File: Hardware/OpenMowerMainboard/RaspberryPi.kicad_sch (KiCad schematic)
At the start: 10 parts, among them J21 Raspberry_Pi_2_3, J22 Conn_02x04_Odd_Even, M1 Fan, Q3 BSS138, U3 SIP32509DT

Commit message: BoM data added to kicad - results exported to .xlsx file
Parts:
- D1: LCSC (none) -> C541613; Part Number (none) -> AS160-M; Stock_PN (none) -> D-AS160-M
- J21: Digikey (none) -> S5729-ND; Part Number (none) -> NPPC202KFMS-RC; Stock_PN (none) -> J-SMD-2x20-.1F
- J22: LCSC (none) -> C2894965; Part Number (none) -> PZ254-2-04-Z-8.5; Stock_PN (none) -> J-TH-2x4-.1
- M1: LCSC (none) -> C2935908; Part Number (none) -> DZ254R-11-02-63; Stock_PN (none) -> J-TH-1x2-.1
- Q3: LCSC (none) -> C360338; Part Number (none) -> AP2300; Stock_PN (none) -> Q-AP2300
- R1, R2, R4: Digikey (none) -> 738-RMCF0805FG10K0CT-ND; Part Number (none) -> RMCF0805FG10K0; Stock_PN (none) -> R-805-10K-.125W-1%
- R5: Digikey (none) -> 311-150CRCT-ND; Part Number (none) -> RC0805FR-07150RL; Stock_PN (none) -> R-805-150-.125W-1%
- U3: Digikey (none) -> SIP32509DT-T1-GE3CT-ND; Part Number (none) -> SIP32509DT-T1-GE3; Stock_PN (none) -> U-SIP32509
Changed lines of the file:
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@@
+      (effects (font (size 1.27 1.27)) hide)
+    )
+    (property "LCSC" "C2935908" (id 4) (at 116.84 36.83 0)
+      (effects (font (size 1.27 1.27)) hide)
+    )
+    (property "Part Number" "DZ254R-11-02-63" (id 5) (at 116.84 36.83 0)
+      (effects (font (size 1.27 1.27)) hide)
+    )
+    (property "Stock_PN" "J-TH-1x2-.1" (id 6) (at 116.84 36.83 0)
       (effects (font (size 1.27 1.27)) hide)
     )
@@
     )
     (property "Datasheet" "~" (id 3) (at 107.95 35.56 0)
+      (effects (font (size 1.27 1.27)) hide)
+    )
+    (property "LCSC" "C541613" (id 4) (at 107.95 35.56 0)
+      (effects (font (size 1.27 1.27)) hide)
+    )
+    (property "Part Number" "AS160-M" (id 5) (at 107.95 35.56 0)
+      (effects (font (size 1.27 1.27)) hide)
+    )
+    (property "Stock_PN" "D-AS160-M" (id 6) (at 107.95 35.56 0)
       (effects (font (size 1.27 1.27)) hide)
     )
@@
     )
     (property "Datasheet" "~" (id 3) (at 184.15 152.4 0)
+      (effects (font (size 1.27 1.27)) hide)
+    )
+    (property "Digikey" "738-RMCF0805FG10K0CT-ND" (id 4) (at 184.15 152.4 0)
+      (effects (font (size 1.27 1.27)) hide)
+    )
+    (property "Part Number" "RMCF0805FG10K0" (id 5) (at 184.15 152.4 0)
+      (effects (font (size 1.27 1.27)) hide)
+    )
+    (property "Stock_PN" "R-805-10K-.125W-1%" (id 6) (at 184.15 152.4 0)
       (effects (font (size 1.27 1.27)) hide)
     )
@@
     )
     (property "Datasheet" "~" (id 3) (at 57.785 144.145 0)
+      (effects (font (size 1.27 1.27)) hide)
+    )
+    (property "LCSC" "C2894965" (id 4) (at 57.785 144.145 0)
+      (effects (font (size 1.27 1.27)) hide)
+    )
+    (property "Part Number" "	PZ254-2-04-Z-8.5" (id 5) (at 57.785 144.145 0)
+      (effects (font (size 1.27 1.27)) hide)
+    )
+    (property "Stock_PN" "J-TH-2x4-.1" (id 6) (at 57.785 144.145 0)
       (effects (font (size 1.27 1.27)) hide)
     )
@@
       (effects (font (size 1.27 1.27)) hide)
     )
+    (property "Digikey" "SIP32509DT-T1-GE3CT-ND" (id 4) (at 166.37 17.78 0)
+      (effects (font (size 1.27 1.27)) hide)
+    )
+    (property "Part Number" "SIP32509DT-T1-GE3" (id 5) (at 166.37 17.78 0)
+      (effects (font (size 1.27 1.27)) hide)
+    )
+    (property "Stock_PN" "U-SIP32509" (id 6) (at 166.37 17.78 0)
+      (effects (font (size 1.27 1.27)) hide)
+    )
     (pin "1")
     (pin "2")
@@
       (effects (font (size 1.27 1.27)) hide)
     )
+    (property "Stock_PN" "R-805-150-.125W-1%" (id 4) (at 101.6 49.53 0)
+      (effects (font (size 1.27 1.27)) hide)
+    )
+    (property "Digikey" "311-150CRCT-ND" (id 5) (at 101.6 49.53 0)
+      (effects (font (size 1.27 1.27)) hide)
+    )
+    (property "Part Number" "RC0805FR-07150RL" (id 6) (at 101.6 49.53 0)
+      (effects (font (size 1.27 1.27)) hide)
+    )
     (pin "1")
     (pin "2")
@@
       (effects (font (size 1.27 1.27)) (justify left) hide)
     )
+    (property "LCSC" "C360338" (id 4) (at 114.3 49.53 0)
+      (effects (font (size 1.27 1.27)) hide)
+    )
+    (property "Part Number" "AP2300" (id 5) (at 114.3 49.53 0)
+      (effects (font (size 1.27 1.27)) hide)
+    )
+    (property "Stock_PN" "Q-AP2300" (id 6) (at 114.3 49.53 0)
+      (effects (font (size 1.27 1.27)) hide)
+    )
     (pin "1")
     (pin "2")
@@
       (effects (font (size 1.27 1.27)) hide)
     )
+    (property "Digikey" "738-RMCF0805FG10K0CT-ND" (id 4) (at 93.98 57.15 0)
+      (effects (font (size 1.27 1.27)) hide)
+    )
+    (property "Part Number" "RMCF0805FG10K0" (id 5) (at 93.98 57.15 0)
+      (effects (font (size 1.27 1.27)) hide)
+    )
+    (property "Stock_PN" "R-805-10K-.125W-1%" (id 6) (at 93.98 57.15 0)
+      (effects (font (size 1.27 1.27)) hide)
+    )
     (pin "1")
     (pin "2")
@@
     )
     (property "Datasheet" "https://www.raspberrypi.org/documentation/hardware/raspberrypi/schematics/rpi_SCH_3bplus_1p0_reduced.pdf" (id 3) (at 107.315 133.985 0)
+      (effects (font (size 1.27 1.27)) hide)
+    )
+    (property "Digikey" "S5729-ND" (id 4) (at 107.315 133.985 0)
+      (effects (font (size 1.27 1.27)) hide)
+    )
+    (property "Part Number" "NPPC202KFMS-RC" (id 5) (at 107.315 133.985 0)
+      (effects (font (size 1.27 1.27)) hide)
+    )
+    (property "Stock_PN" "J-SMD-2x20-.1F" (id 6) (at 107.315 133.985 0)
       (effects (font (size 1.27 1.27)) hide)
     )
@@
       (effects (font (size 1.27 1.27)) hide)
     )
+    (property "Digikey" "738-RMCF0805FG10K0CT-ND" (id 4) (at 184.15 130.175 0)
+      (effects (font (size 1.27 1.27)) hide)
+    )
+    (property "Part Number" "RMCF0805FG10K0" (id 5) (at 184.15 130.175 0)
+      (effects (font (size 1.27 1.27)) hide)
+    )
+    (property "Stock_PN" "R-805-10K-.125W-1%" (id 6) (at 184.15 130.175 0)
+      (effects (font (size 1.27 1.27)) hide)
+    )

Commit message: BOM changes
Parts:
- added JP7, JP8: SolderJumper_2_Bridged, Jumper:SolderJumper-2_P1.3mm_Bridged_RoundedPad1.0x1.5mm, symbol Jumper:SolderJumper_2_Bridged
- D1: Digikey (none) -> 3757-SS0520_R1_00001CT-ND
- Q3: Digikey (none) -> BSS138K-13DICT-ND
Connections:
- net PICO_SWCLK: now also JP8.1 (A)
- net PICO_SWDIO: now also JP7.1 (A)
- net at J21.18 (GPIO24), J22.4 (Pin_4): now also JP7.2 (B)
- net at J21.22 (GPIO25), J22.6 (Pin_6): now also JP8.2 (B)
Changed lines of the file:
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@@
   (junction (at 106.045 171.45) (diameter 0) (color 0 0 0 0)
   )
+  (junction (at 67.31 144.145) (diameter 0) (color 0 0 0 0)
+  )
+  (junction (at 68.58 146.685) (diameter 0) (color 0 0 0 0)
+  )
   (junction (at 102.235 98.425) (diameter 0) (color 0 0 0 0)
   )
@@
   (junction (at 109.855 171.45) (diameter 0) (color 0 0 0 0)
   )
+  (junction (at 49.53 146.685) (diameter 0) (color 0 0 0 0)
+  )
   (junction (at 104.775 171.45) (diameter 0) (color 0 0 0 0)
   )
@@
   )
   (junction (at 184.15 144.145) (diameter 0) (color 0 0 0 0)
+  )
+  (junction (at 50.8 144.145) (diameter 0) (color 0 0 0 0)
   )
   (junction (at 112.395 171.45) (diameter 0) (color 0 0 0 0)
@@
     (stroke (width 0) (type default) (color 0 0 0 0))
   )
+  (wire (pts (xy 68.58 130.175) (xy 68.58 146.685))
+    (stroke (width 0) (type default) (color 0 0 0 0))
+  )
   (wire (pts (xy 196.85 38.1) (xy 196.85 67.31))
     (stroke (width 0) (type default) (color 0 0 0 0))
@@
     (stroke (width 0) (type default) (color 0 0 0 0))
   )
-  (wire (pts (xy 46.99 146.685) (xy 52.705 146.685))
+  (wire (pts (xy 55.245 127) (xy 50.8 127))
+    (stroke (width 0) (type default) (color 0 0 0 0))
+  )
+  (wire (pts (xy 46.99 146.685) (xy 49.53 146.685))
+    (stroke (width 0) (type default) (color 0 0 0 0))
+  )
+  (wire (pts (xy 67.31 127) (xy 67.31 144.145))
     (stroke (width 0) (type default) (color 0 0 0 0))
   )
@@
     (stroke (width 0) (type default) (color 0 0 0 0))
   )
+  (wire (pts (xy 50.8 127) (xy 50.8 144.145))
+    (stroke (width 0) (type default) (color 0 0 0 0))
+  )
   (wire (pts (xy 102.235 100.965) (xy 102.235 98.425))
     (stroke (width 0) (type default) (color 0 0 0 0))
@@
     (stroke (width 0) (type default) (color 0 0 0 0))
   )
-  (wire (pts (xy 65.405 144.145) (xy 86.995 144.145))
-    (stroke (width 0) (type default) (color 0 0 0 0))
-  )
-  (wire (pts (xy 46.99 144.145) (xy 52.705 144.145))
+  (wire (pts (xy 65.405 144.145) (xy 67.31 144.145))
+    (stroke (width 0) (type default) (color 0 0 0 0))
+  )
+  (wire (pts (xy 46.99 144.145) (xy 50.8 144.145))
     (stroke (width 0) (type default) (color 0 0 0 0))
   )
@@
     (stroke (width 0) (type default) (color 0 0 0 0))
   )
+  (wire (pts (xy 49.53 146.685) (xy 52.705 146.685))
+    (stroke (width 0) (type default) (color 0 0 0 0))
+  )
   (wire (pts (xy 107.315 167.005) (xy 107.315 171.45))
     (stroke (width 0) (type default) (color 0 0 0 0))
   )
+  (wire (pts (xy 50.8 144.145) (xy 52.705 144.145))
+    (stroke (width 0) (type default) (color 0 0 0 0))
+  )
   (wire (pts (xy 191.77 49.53) (xy 199.39 49.53))
     (stroke (width 0) (type default) (color 0 0 0 0))
@@
     (stroke (width 0) (type default) (color 0 0 0 0))
   )
+  (wire (pts (xy 68.58 146.685) (xy 86.995 146.685))
+    (stroke (width 0) (type default) (color 0 0 0 0))
+  )
   (wire (pts (xy 127.635 151.765) (xy 150.495 151.765))
     (stroke (width 0) (type default) (color 0 0 0 0))
@@
     (stroke (width 0) (type default) (color 0 0 0 0))
   )
-  (wire (pts (xy 65.405 146.685) (xy 86.995 146.685))
+  (wire (pts (xy 65.405 146.685) (xy 68.58 146.685))
     (stroke (width 0) (type default) (color 0 0 0 0))
   )
@@
     (stroke (width 0) (type default) (color 0 0 0 0))
   )
+  (wire (pts (xy 67.31 144.145) (xy 86.995 144.145))
+    (stroke (width 0) (type default) (color 0 0 0 0))
+  )
   (wire (pts (xy 93.98 60.96) (xy 93.98 64.77))
     (stroke (width 0) (type default) (color 0 0 0 0))
@@
     (stroke (width 0) (type default) (color 0 0 0 0))
   )
+  (wire (pts (xy 62.865 127) (xy 67.31 127))
+    (stroke (width 0) (type default) (color 0 0 0 0))
+  )
   (wire (pts (xy 160.02 46.99) (xy 163.83 46.99))
     (stroke (width 0) (type default) (color 0 0 0 0))
@@
     (stroke (width 0) (type default) (color 0 0 0 0))
   )
+  (wire (pts (xy 49.53 130.175) (xy 49.53 146.685))
+    (stroke (width 0) (type default) (color 0 0 0 0))
+  )
   (wire (pts (xy 102.235 171.45) (xy 104.775 171.45))
     (stroke (width 0) (type default) (color 0 0 0 0))
@@
   )
   (wire (pts (xy 97.155 171.45) (xy 99.695 171.45))
+    (stroke (width 0) (type default) (color 0 0 0 0))
+  )
+  (wire (pts (xy 55.245 130.175) (xy 49.53 130.175))
+    (stroke (width 0) (type default) (color 0 0 0 0))
+  )
+  (wire (pts (xy 62.865 130.175) (xy 68.58 130.175))
     (stroke (width 0) (type default) (color 0 0 0 0))
   )
@@
     )
     (property "Stock_PN" "D-AS160-M" (id 6) (at 107.95 35.56 0)
+      (effects (font (size 1.27 1.27)) hide)
+    )
+    (property "Digikey" "3757-SS0520_R1_00001CT-ND" (id 7) (at 107.95 35.56 0)
+      (effects (font (size 1.27 1.27)) hide)
+    )
+    (pin "1")
+    (pin "2")
+  )
+  (symbol (lib_id "Jumper:SolderJumper_2_Bridged") (at 59.055 130.175 0) (unit 1)
+    (in_bom no) (on_board yes)
+    (property "Reference" "JP8" (id 0) (at 59.055 124.46 0))
+    (property "Value" "SolderJumper_2_Bridged" (id 1) (at 59.055 132.08 0))
+    (property "Footprint" "Jumper:SolderJumper-2_P1.3mm_Bridged_RoundedPad1.0x1.5mm" (id 2) (at 59.055 130.175 0)
+      (effects (font (size 1.27 1.27)) hide)
+    )
+    (property "Datasheet" "~" (id 3) (at 59.055 130.175 0)
       (effects (font (size 1.27 1.27)) hide)
     )
@@
     (pin "1")
   )
+  (symbol (lib_id "Jumper:SolderJumper_2_Bridged") (at 59.055 127 0) (unit 1)
+    (in_bom no) (on_board yes)
+    (property "Reference" "JP7" (id 0) (at 59.055 121.285 0))
+    (property "Value" "SolderJumper_2_Bridged" (id 1) (at 59.055 125.095 0))
+    (property "Footprint" "Jumper:SolderJumper-2_P1.3mm_Bridged_RoundedPad1.0x1.5mm" (id 2) (at 59.055 127 0)
+      (effects (font (size 1.27 1.27)) hide)
+    )
+    (property "Datasheet" "~" (id 3) (at 59.055 127 0)
+      (effects (font (size 1.27 1.27)) hide)
+    )
+    (pin "1")
+    (pin "2")
+  )
   (symbol (lib_id "power:GND") (at 68.58 154.305 0) (unit 1)
     (in_bom yes) (on_board yes)
@@
       (effects (font (size 1.27 1.27)) hide)
     )
+    (property "Digikey" "BSS138K-13DICT-ND" (id 7) (at 114.3 49.53 0)
+      (effects (font (size 1.27 1.27)) hide)
+    )

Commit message: chore: remove space before PN
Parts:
- J22: Part Number PZ254-2-04-Z-8.5 -> PZ254-2-04-Z-8.5
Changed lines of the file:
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@@
       (effects (font (size 1.27 1.27)) hide)
     )
-    (property "Part Number" "	PZ254-2-04-Z-8.5" (id 5) (at 57.785 144.145 0)
+    (property "Part Number" "PZ254-2-04-Z-8.5" (id 5) (at 57.785 144.145 0)
       (effects (font (size 1.27 1.27)) hide)
     )

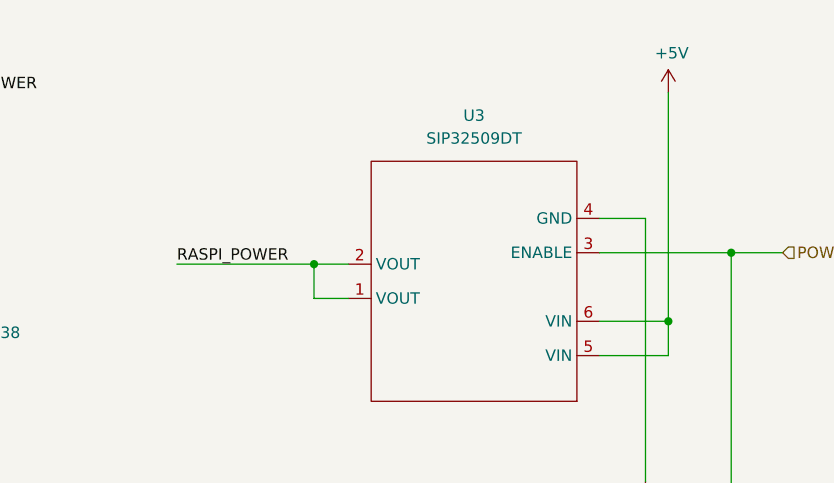
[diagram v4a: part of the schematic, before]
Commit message: feat: add SW1 RPi power-on switch
Fixes #40
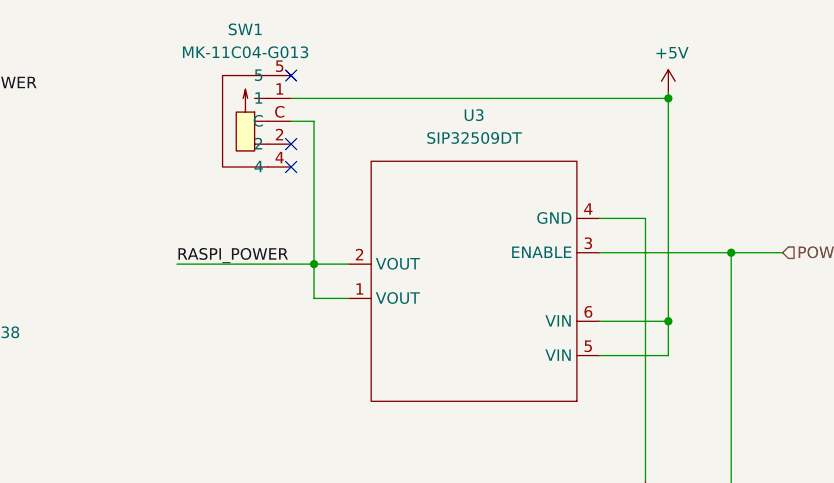
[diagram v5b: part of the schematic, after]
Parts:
- added SW1: MK-11C04-G013, lcsc:SW-SMD_MK-11C04-G013, symbol lcsc:MK-11C04-G013
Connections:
- net +5V: now also SW1.1
- net RASPI_POWER: now also SW1.C
- no-connect marks 15 -> 18
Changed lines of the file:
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@@
   (junction (at 116.84 43.18) (diameter 0) (color 0 0 0 0)
   )
+  (junction (at 199.39 24.765) (diameter 0) (color 0 0 0 0)
+  )
   (junction (at 102.235 171.45) (diameter 0) (color 0 0 0 0)
   )
@@
   (junction (at 206.375 41.91) (diameter 0) (color 0 0 0 0)
   )
+  (no_connect (at 157.48 32.385))
+  (no_connect (at 157.48 29.845))
   (no_connect (at 127.635 121.285))
   (no_connect (at 127.635 118.745))
@@
   (no_connect (at 127.635 146.685))
   (no_connect (at 127.635 136.525))
+  (no_connect (at 157.48 22.225))
   (wire (pts (xy 158.115 111.125) (xy 127.635 111.125))
     (stroke (width 0) (type default) (color 0 0 0 0))
@@
     (stroke (width 0) (type default) (color 0 0 0 0))
   )
+  (wire (pts (xy 157.48 24.765) (xy 199.39 24.765))
+    (stroke (width 0) (type default) (color 0 0 0 0))
+  )
   (wire (pts (xy 199.39 53.34) (xy 199.39 49.53))
     (stroke (width 0) (type default) (color 0 0 0 0))
@@
     (stroke (width 0) (type default) (color 0 0 0 0))
   )
+  (wire (pts (xy 157.48 27.305) (xy 160.02 27.305))
+    (stroke (width 0) (type default) (color 0 0 0 0))
+  )
   (wire (pts (xy 158.115 141.605) (xy 127.635 141.605))
     (stroke (width 0) (type default) (color 0 0 0 0))
@@
     (stroke (width 0) (type default) (color 0 0 0 0))
   )
+  (wire (pts (xy 160.02 27.305) (xy 160.02 43.18))
+    (stroke (width 0) (type default) (color 0 0 0 0))
+  )
+  (wire (pts (xy 199.39 24.765) (xy 199.39 49.53))
+    (stroke (width 0) (type default) (color 0 0 0 0))
+  )
   (wire (pts (xy 160.02 43.18) (xy 160.02 46.99))
     (stroke (width 0) (type default) (color 0 0 0 0))
@@
     (stroke (width 0) (type default) (color 0 0 0 0))
   )
-  (wire (pts (xy 199.39 24.13) (xy 199.39 49.53))
+  (wire (pts (xy 199.39 24.13) (xy 199.39 24.765))
     (stroke (width 0) (type default) (color 0 0 0 0))
   )
@@
     (pin "6")
   )
+  (symbol (lib_id "lcsc:MK-11C04-G013") (at 152.4 27.305 270) (unit 1)
+    (in_bom yes) (on_board yes) (fields_autoplaced)
+    (property "Reference" "SW1" (id 0) (at 152.4 17.145 90))
+    (property "Value" "MK-11C04-G013" (id 1) (at 152.4 19.685 90))
+    (property "Footprint" "lcsc:SW-SMD_MK-11C04-G013" (id 2) (at 149.86 27.305 0)
+      (effects (font (size 1.27 1.27)) hide)
+    )
+    (property "Datasheet" "https://lcsc.com/product-detail/Toggle-Switches_G-Switch-MK-11C04-G013_C778185.html" (id 3) (at 147.32 27.305 0)
+      (effects (font (size 1.27 1.27)) hide)
+    )
+    (property "Manufacturer" "G-Switch" (id 4) (at 144.78 27.305 0)
+      (effects (font (size 1.27 1.27)) hide)
+    )
+    (property "LCSC Part" "C778185" (id 5) (at 142.24 27.305 0)
+      (effects (font (size 1.27 1.27)) hide)
+    )
+    (property "JLC Part" "Extended Part" (id 6) (at 139.7 27.305 0)
+      (effects (font (size 1.27 1.27)) hide)
+    )
+    (pin "1")
+    (pin "2")
+    (pin "4")
+    (pin "5")
+    (pin "C")
+  )
   (symbol (lib_id "Device:R") (at 101.6 49.53 90) (unit 1)

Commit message: chore: duplicate `LCSC Part` to LCSC
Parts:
- SW1: LCSC (none) -> C778185
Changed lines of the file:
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@@
+      (effects (font (size 1.27 1.27)) hide)
+    )
+    (property "LCSC" "C778185" (id 7) (at 152.4 27.305 0)
       (effects (font (size 1.27 1.27)) hide)
     )

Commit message: feat(imu): deprecate WT901 and MPU9250 (J20)
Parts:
- J21: footprint Connector_PinSocket_2.54mm:PinSocket_2x20_P2.54mm_Vertical_SMD -> lcsc:HDR-SMD_40P-P2.54-V-F-R2-C20-S8.8-EH
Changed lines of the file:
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@@
       (effects (font (size 1.27 1.27)) (justify left))
     )
-    (property "Footprint" "Connector_PinSocket_2.54mm:PinSocket_2x20_P2.54mm_Vertical_SMD" (id 2) (at 107.315 133.985 0)
+    (property "Footprint" "lcsc:HDR-SMD_40P-P2.54-V-F-R2-C20-S8.8-EH" (id 2) (at 107.315 133.985 0)
       (effects (font (size 1.27 1.27)) hide)
     )
